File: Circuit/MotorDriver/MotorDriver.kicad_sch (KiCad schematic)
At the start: 28 parts, among them J3 Conn_01x03_Pin, J4 Conn_01x04_Pin, J5 Conn_01x06_Pin, J6 Conn_01x02_Pin, U3 DRV8316RRGFR, U4 XC6206PxxxMR

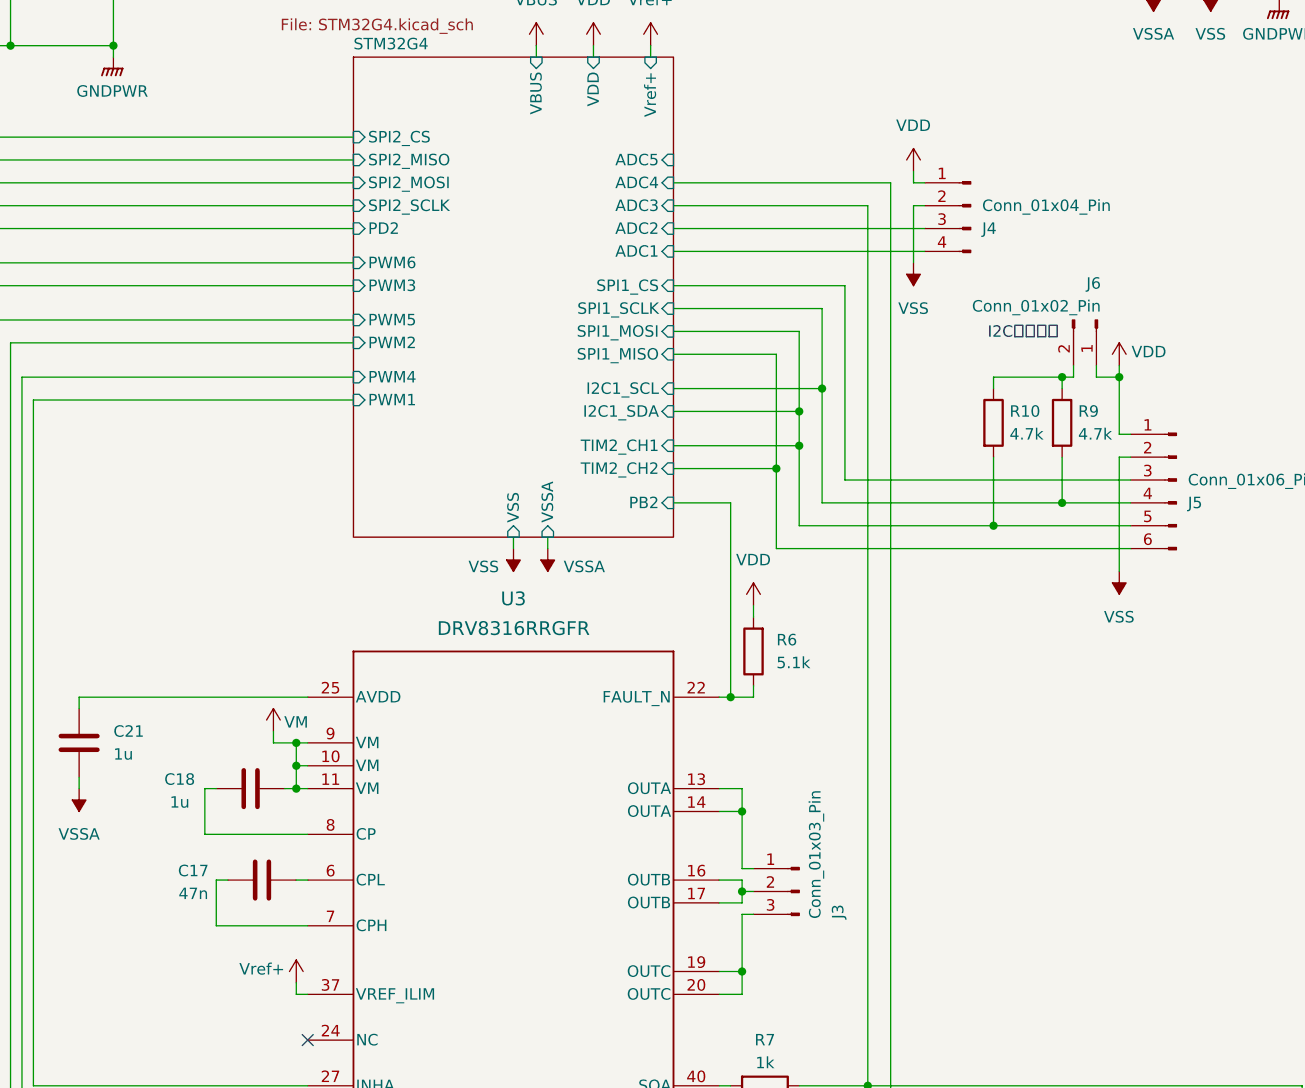
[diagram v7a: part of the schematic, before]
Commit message: 3相部分を除きフットプリント割り当て完了
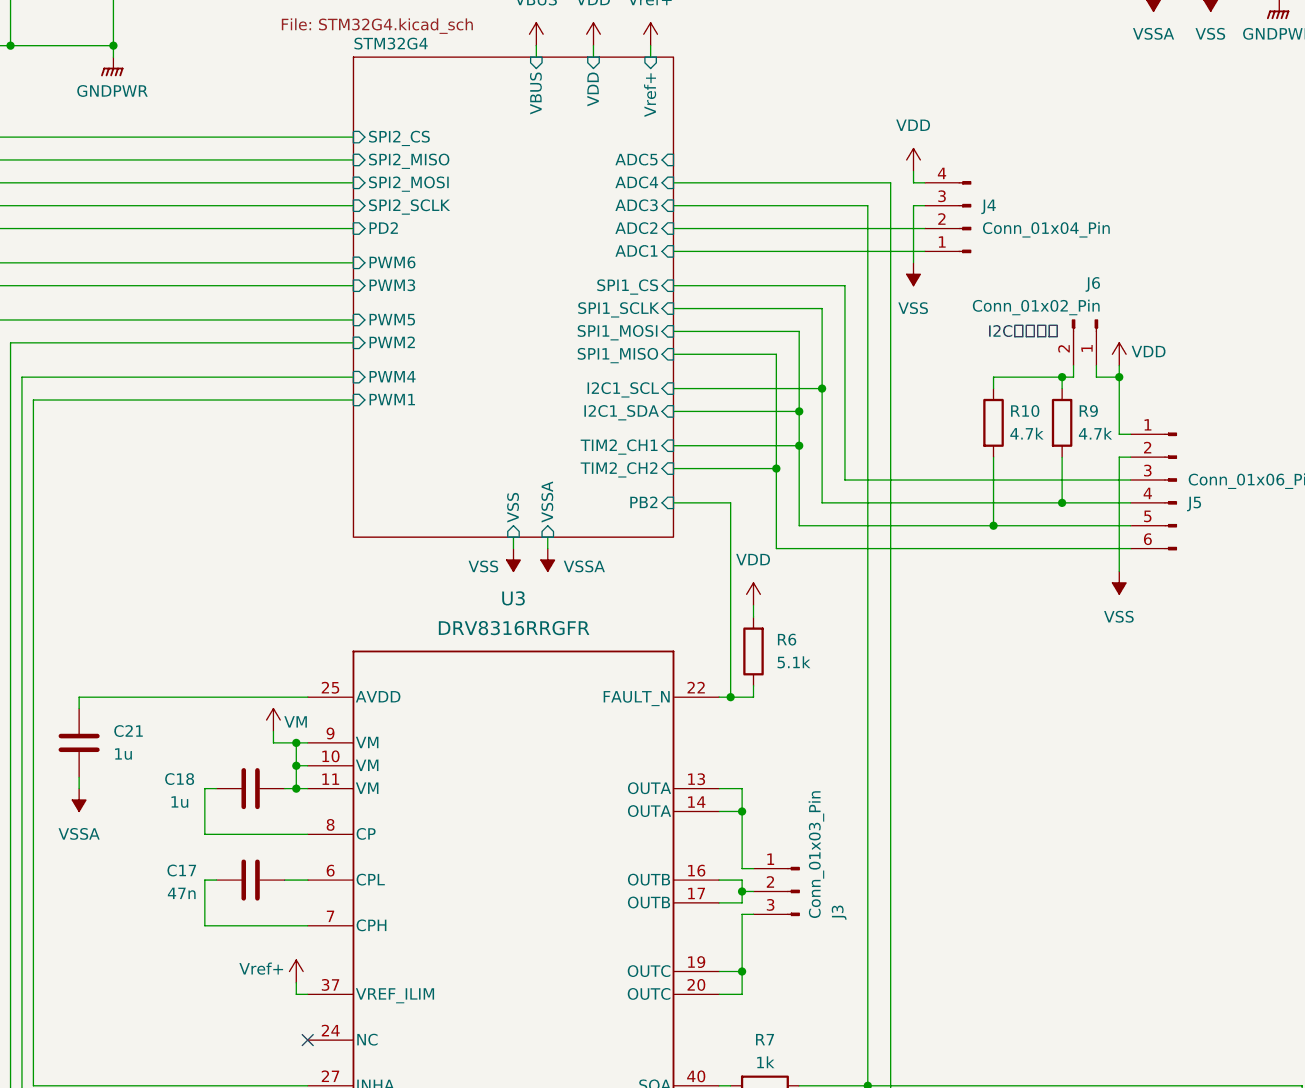
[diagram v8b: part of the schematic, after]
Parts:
- J4: footprint (none) -> Connector_JST:JST_GH_SM04B-GHS-TB_1x04-1MP_P1.25mm_Horizontal
- J5: footprint (none) -> OU_conn:Hirose_DF1EC-6P-2.5DSA
- J6: footprint (none) -> Connector_PinHeader_2.54mm:PinHeader_1x02_P2.54mm_Vertical
- U3: footprint RGF0040E-IPC_A -> OU_Power:DRV8316RRGFR
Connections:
- net STM32G4/ADC1: now also J4.1 (Pin_1); no longer J4.4 (Pin_4)
- net STM32G4/ADC2: now also J4.2 (Pin_2); no longer J4.3 (Pin_3)
- net VDD: now also J4.4 (Pin_4); no longer J4.1 (Pin_1)
- net VSS: now also J4.3 (Pin_3); no longer J4.2 (Pin_2)
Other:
- moved on the sheet: C17, J4
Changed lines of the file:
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@@
 	(wire
 		(pts
+			(xy 144.78 64.77) (xy 146.05 64.77)
+		)
+		(stroke
+			(width 0)
+			(type default)
+		)
+	)
+	(wire
+		(pts
 			(xy 124.46 213.36) (xy 134.62 213.36)
 		)
@@
 	(wire
 		(pts
-			(xy 144.78 64.77) (xy 146.05 64.77)
-		)
-		(stroke
-			(width 0)
-			(type default)
-		)
-	)
-	(wire
-		(pts
 			(xy 118.11 91.44) (xy 132.08 91.44)
 		)
@@
 	(wire
 		(pts
-			(xy 68.58 139.7) (xy 67.31 139.7)
+			(xy 67.31 139.7) (xy 66.04 139.7)
 		)
 		(stroke
@@
 	(wire
 		(pts
-			(xy 146.05 62.23) (xy 144.78 62.23)
+			(xy 125.73 129.54) (xy 123.19 129.54)
 		)
 		(stroke
@@
 	(wire
 		(pts
-			(xy 125.73 129.54) (xy 123.19 129.54)
+			(xy 144.78 62.23) (xy 146.05 62.23)
 		)
 		(stroke
@@
 	(wire
 		(pts
-			(xy 67.31 139.7) (xy 67.31 144.78)
+			(xy 66.04 139.7) (xy 66.04 144.78)
 		)
 		(stroke
@@
 	(wire
 		(pts
-			(xy 67.31 144.78) (xy 77.47 144.78)
+			(xy 66.04 144.78) (xy 77.47 144.78)
 		)
 		(stroke
@@
 	(wire
 		(pts
+			(xy 118.11 67.31) (xy 146.05 67.31)
+		)
+		(stroke
+			(width 0)
+			(type default)
+		)
+	)
+	(wire
+		(pts
 			(xy 102.87 46.99) (xy 102.87 48.26)
 		)
@@
 	(wire
 		(pts
-			(xy 76.2 139.7) (xy 77.47 139.7)
+			(xy 74.93 139.7) (xy 77.47 139.7)
 		)
 		(stroke
@@
 	(wire
 		(pts
-			(xy 118.11 67.31) (xy 146.05 67.31)
-		)
-		(stroke
-			(width 0)
-			(type default)
-		)
-	)
-	(wire
-		(pts
 			(xy 144.78 64.77) (xy 144.78 71.12)
 		)
@@
 	(symbol
 		(lib_id "Device:C")
-		(at 72.39 139.7 270)
+		(at 71.12 139.7 270)
 		(unit 1)
 		(body_style 1)
@@
 		(dnp no)
 		(property "Reference" "C17"
-			(at 64.77 138.684 90)
+			(at 63.5 138.684 90)
 			(show_name no)
 			(do_not_autoplace no)
@@
 		)
 		(property "Value" "47n"
-			(at 64.77 141.224 90)
+			(at 63.5 141.224 90)
 			(show_name no)
 			(do_not_autoplace no)
@@
 		)
 		(property "Footprint" "Capacitor_SMD:C_0603_1608Metric"
-			(at 68.58 140.6652 0)
+			(at 67.31 140.6652 0)
 			(hide yes)
 			(show_name no)
@@
 		)
 		(property "Datasheet" ""
-			(at 72.39 139.7 0)
+			(at 71.12 139.7 0)
 			(hide yes)
 			(show_name no)
@@
 		)
 		(property "Description" "Unpolarized capacitor"
-			(at 72.39 139.7 0)
+			(at 71.12 139.7 0)
 			(hide yes)
 			(show_name no)
@@
 			)
 		)
-		(property "Footprint" ""
+		(property "Footprint" "OU_conn:Hirose_DF1EC-6P-2.5DSA"
 			(at 173.99 95.25 0)
 			(hide yes)
@@
 	(symbol
 		(lib_id "Connector:Conn_01x04_Pin")
-		(at 151.13 64.77 0)
-		(mirror y)
+		(at 151.13 67.31 180)
 		(unit 1)
 		(body_style 1)
@@
 		(dnp no)
 		(property "Reference" "J4"
-			(at 152.4 67.3101 0)
+			(at 152.4 64.7699 0)
 			(show_name no)
 			(do_not_autoplace no)
@@
 		)
 		(property "Value" "Conn_01x04_Pin"
-			(at 152.4 64.7701 0)
+			(at 152.4 67.3099 0)
 			(show_name no)
 			(do_not_autoplace no)
@@
 			)
 		)
-		(property "Footprint" ""
-			(at 151.13 64.77 0)
+		(property "Footprint" "Connector_JST:JST_GH_SM04B-GHS-TB_1x04-1MP_P1.25mm_Horizontal"
+			(at 151.13 67.31 0)
 			(hide yes)
 			(show_name no)
@@
 		)
 		(property "Datasheet" ""
-			(at 151.13 64.77 0)
+			(at 151.13 67.31 0)
 			(hide yes)
 			(show_name no)
@@
 		)
 		(property "Description" "Generic connector, single row, 01x04, script generated"
-			(at 151.13 64.77 0)
+			(at 151.13 67.31 0)
 			(hide yes)
 			(show_name no)
@@
 			)
 		)
-		(property "Footprint" "RGF0040E-IPC_A"
+		(property "Footprint" "OU_Power:DRV8316RRGFR"
 			(at 77.47 119.38 0)
 			(hide yes)
@@
 			)
 		)
-		(property "Footprint" ""
+		(property "Footprint" "Connector_PinHeader_2.54mm:PinHeader_1x02_P2.54mm_Vertical"
 			(at 165.1 77.47 0)
 			(hide yes)
